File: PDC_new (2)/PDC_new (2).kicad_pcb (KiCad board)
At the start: 2 copper layers, 96 parts, among them J1 Conn_01x02_Pin, J10 Conn_01x02_Pin, J12 Conn_01x02_Pin, J13 XT90PW-F, J14 B2B-XH-A__LF__SN_, J15 Conn_01x02, J2 Conn_01x02_Pin, J3 Conn_01x02_Pin, J4 Conn_01x02_Pin, J5 Conn_01x02_Pin, J6 Conn_01x02_Pin, J7 Conn_01x02_Pin, J8 Conn_01x02_Pin, J9 Conn_01x02_Pin, Q1 BSS123, Q2 IRF540NSTRLPBF, U1 TPSI3050QDWZRQ1, U10 LM393LVDR, U11 IPB017N10N5ATMA1, U12 IPB017N10N5ATMA1, U14 IPB017N10N5ATMA1, U2 TPSI3050QDWZRQ1, U3 TPSI3050QDWZRQ1, U4 74HC74, U5 URB4805LD-60WR3, U6 IPB017N10N5ATMA1, U7 TLC555CDR, U8 SN74HC08D, U9 SN74HC14DR

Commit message: Route PDC_new (2) PCB and swap JST/switch for XT90PW(2+2) connector
Schematic:
- Replace the two JST XH (B2B-XH-A) connectors and the TS-1187A
  tactile switch with a single XT90PW(2+2)-M.G.Y power+signal connector
- Update related passives, power symbols and net labels

PCB:
- Sync footprints with the schematic (drop JST XH and TS-1187A,
  add CONN-TH_XT90PW2X2-MGY)
- Add first routing pass: ~290 track segments and 6 copper zones

Project:
- Adjust design rules: hole clearance 0.25 mm, min via 0.5 mm /
  0.1 mm annular ring, min text 0.8 mm / 0.08 mm thickness
- Clear predefined track width and diff-pair presets

Co-Authored-By: Claude Opus 5.5 <noreply@anthropic.com>
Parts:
- removed C24: 2.2µF, Capacitor_SMD:C_0805_2012Metric
- removed J14: B2B-XH-A__LF__SN_, Connector_JST:JST_XH_B2B-XH-A_1x02_P2.50mm_Vertical
- removed J15: Conn_01x02, Connector_JST:JST_XH_B2B-XH-A_1x02_P2.50mm_Vertical
- removed R28, R29: 10k, Resistor_SMD:R_0805_2012Metric
- removed S1: TS-1187A-B-A-B, TS-1187A-B-A-B:SW_TS-1187A-B-A-B
- added J11: XT90PW(2+2)-M.G.Y, XT90PW(2+2)-M.G.Y:CONN-TH_XT90PW2X2-MGY, F.Cu at (331.0, 272.4)
- moved C2 261.8 mm to (327.0, 187.8)
- moved C1 261.6 mm to (326.9, 167.9)
- moved C3 261.0 mm to (314.5, 227.0), turned to 90 degrees
- moved C4 258.4 mm to (330.5, 212.0), turned to 90 degrees
- moved D3 241.1 mm to (342.3, 223.5), turned to 90 degrees
- moved D1 238.3 mm to (337.8, 223.5), turned to 90 degrees
- moved D7 233.3 mm to (331.5, 256.5)
- moved U5 230.0 mm to (301.0, 249.0), turned to 180 degrees
- moved C6 218.4 mm to (344.3, 240.7), turned to -90 degrees
- moved C5 216.9 mm to (257.7, 268.1), turned to 180 degrees
- moved J12 216.1 mm to (274.5, 267.9), turned to 180 degrees
- moved R2 212.7 mm to (311.1, 208.7), turned to 90 degrees
- moved R31 212.6 mm to (331.5, 261.0), turned to -90 degrees
- moved F2 206.7 mm to (335.2, 231.5), turned to -90 degrees
- moved J6 202.7 mm to (215.2, 251.6), turned to 90 degrees
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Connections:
- F3 pad 1: /BATT+ -> /PRE_FUSE
- F3 pad 2: /PRE_FUSE -> /BATT+
- R25 pad 1: Net-(U10A-OUT1) -> /CMP_FILT
- R25 pad 2: /CMP_FILT -> Net-(U10A-OUT1)
- RV1 pad 2: Net-(U5-0V) -> GND
- RV1 pad 3: Net-(U5-0V) -> GND
- U11 pad 4: /BATT+ -> /BUS+
- U11 pad 7: /BUS+ -> /BATT+
- U12 pad 4: /BATT+ -> /BUS+
- U12 pad 7: /BUS+ -> /BATT+
- U14 pad 4: /BATT+ -> /BUS+
- U14 pad 7: /BUS+ -> /BATT+
- U5 pad 5: Net-(U5-0V) -> GND
- U6 pad 4: /BATT+ -> /BUS+
- U6 pad 7: /BUS+ -> /BATT+
- U9 pad 5: /MSTR_FILT -> GND
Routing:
- net /EN_BLEED: track 0.00 -> 60.9 mm
- net /GATE_MAIN: track 0.00 -> 47.1 mm
- net /RUN_N: track 0.00 -> 44.8 mm
- net /POR_N: track 0.00 -> 41.4 mm
- net /MSTR_ON: track 0.00 -> 38.7 mm
- net /FAULT_N: track 0.00 -> 32.1 mm
- net /PRE_DRAIN: track 0.00 -> 27.2 mm
- net /DONE_N: track 0.00 -> 26.9 mm
- net /BUCK_IN: track 0.00 -> 21.4 mm
- net /EN_MAIN: track 0.00 -> 20.5 mm
- net Net-(D6-K): track 0.00 -> 18.0 mm
- net /RUN_OK: track 0.00 -> 17.7 mm
- net /RUN_CLR_N: track 0.00 -> 15.2 mm
- net /BUCK_OR: track 0.00 -> 15.0 mm
- net /PRE_FUSE: track 0.00 -> 14.1 mm
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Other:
- board outline added: 153 x 129 mm
- copper layers 2 -> 4

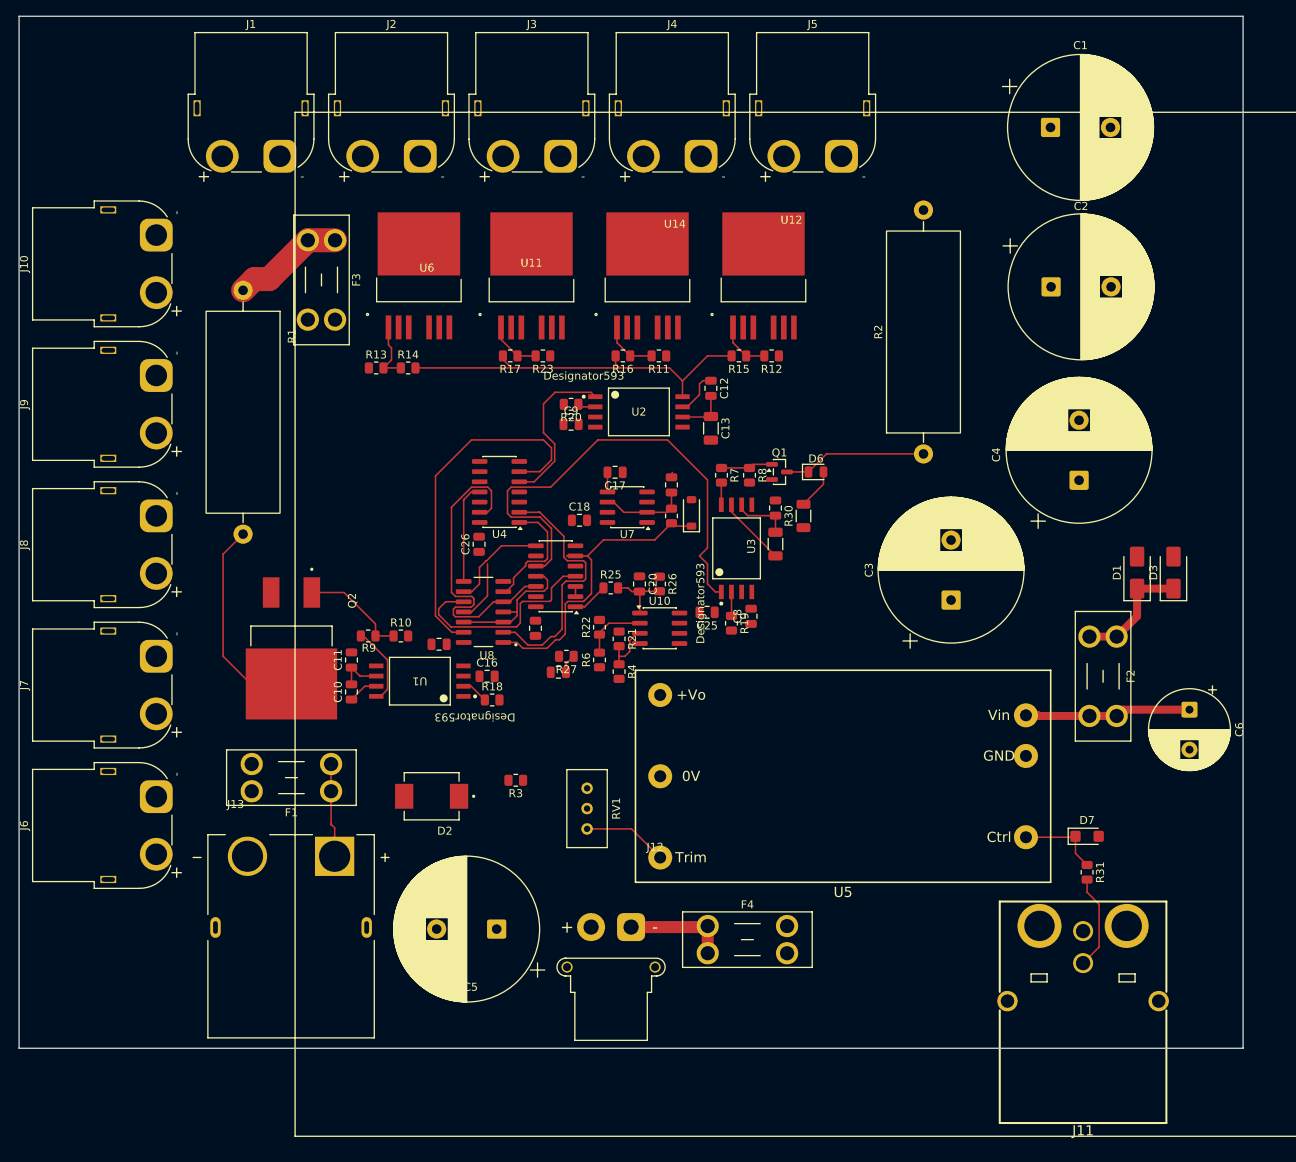
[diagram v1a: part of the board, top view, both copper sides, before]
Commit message: Update PDC_new (2) PCB layout: reposition footprints and reroute tracks
Adjust component placement and silkscreen/graphics, and re-route
affected track segments to match the updated placement.

Co-Authored-By: Claude Opus 5.5 <noreply@anthropic.com>
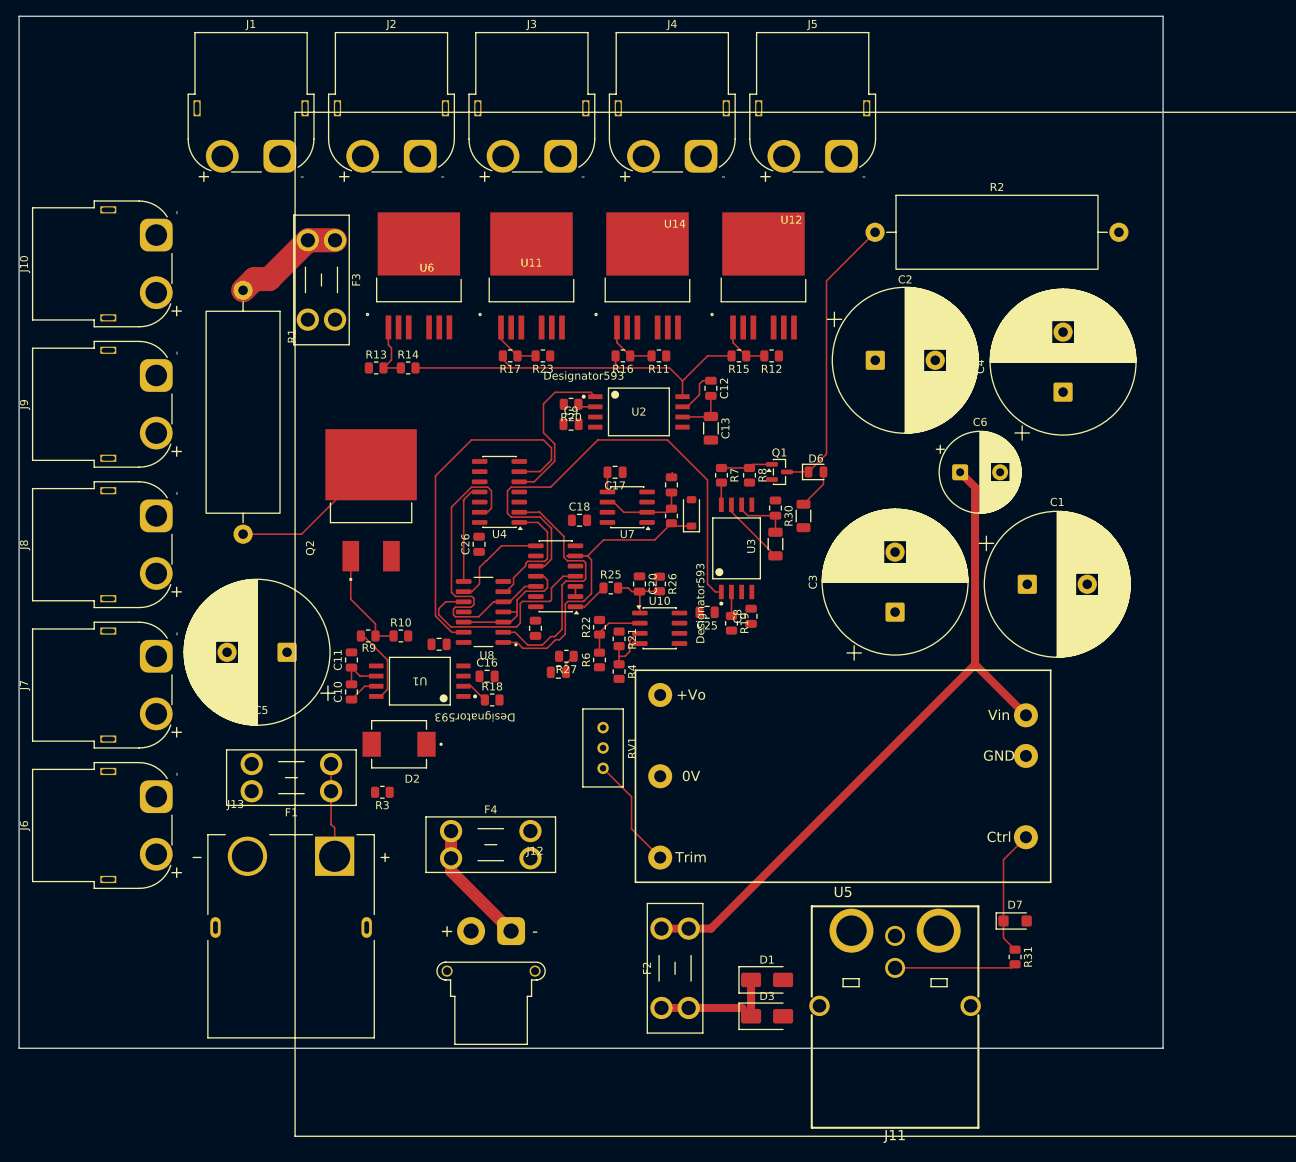
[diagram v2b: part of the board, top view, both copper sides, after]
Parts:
- moved D3 75.2 mm to (291.5, 279.0), turned to 0 degrees
- moved F2 73.4 mm to (278.3, 278.0), turned to 90 degrees
- moved D1 68.8 mm to (291.5, 274.4), turned to 0 degrees
- moved C1 57.2 mm to (324.0, 225.0)
- moved C5 43.4 mm to (231.5, 233.5)
- moved C6 41.3 mm to (315.6, 211.0), turned to 0 degrees
- moved F4 34.2 mm to (252.0, 255.8)
- moved R2 28.4 mm to (305.0, 181.0), turned to 0 degrees
- moved C2 23.8 mm to (305.0, 197.0)
- moved J11 23.5 mm to (307.5, 273.0)
- moved Q2 21.0 mm to (242.0, 214.5), turned to 90 degrees
- moved R3 16.7 mm to (243.4, 251.0)
- moved J12 15.0 mm to (259.5, 268.4)
- moved D7 13.9 mm to (322.5, 267.1)
- moved R31 13.9 mm to (322.5, 271.6)
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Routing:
- net /BUCK_IN: track 21.4 -> 86.9 mm
- net Net-(D6-K): track 18.0 -> 36.1 mm
- net /EN_PRE: track 8.40 -> 0.60 mm
- net /PRE_DRAIN: track 27.2 -> 20.5 mm
- net Net-(J12-Pin_1): track 13.0 -> 19.0 mm
- net /BUCK_CTRL: track 10.4 -> 15.8 mm
- net Net-(U5-Trim): track 10.6 -> 14.1 mm
- net /DET: track 11.9 -> 15.2 mm
- net /BUCK_OR: track 15.0 -> 16.2 mm
- net /EN_BLEED: track 60.9 -> 60.1 mm
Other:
- board size 153 x 129 mm -> 143 x 129 mm

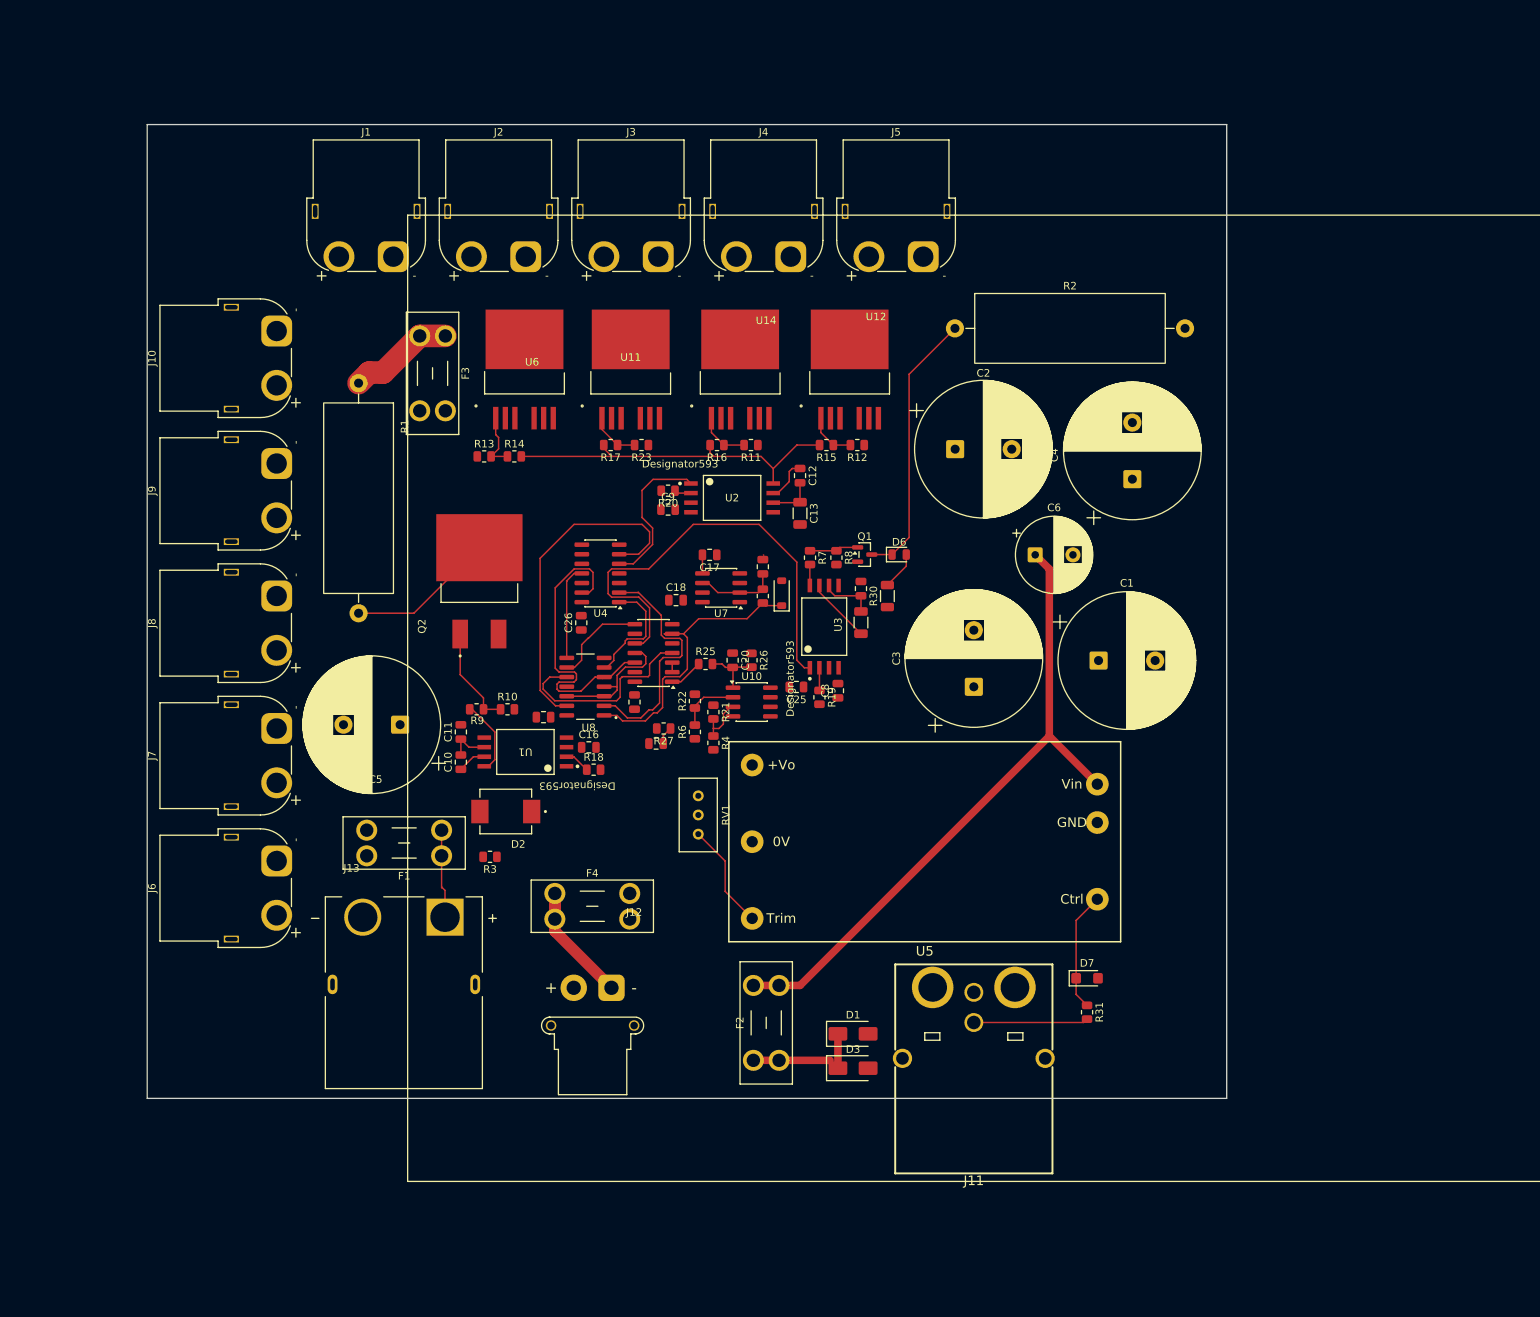
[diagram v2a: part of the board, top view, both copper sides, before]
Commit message: Update PDC_new (2) PCB layout and add XT90PW(2+2) / power part libraries
- Continue routing and layout work on PDC_new (2).kicad_pcb
- Add XT90PW(2+2)-M.G.Y connector symbol/footprint source files
- Add UltraLibrarian import guides for IPB017N10N5ATMA1 and TPSI3050QDWZRQ1
- Ignore 3D model files (*.step, *.stp, *.wrl) so they stay local

Co-Authored-By: Claude Opus 5.5 <noreply@anthropic.com>
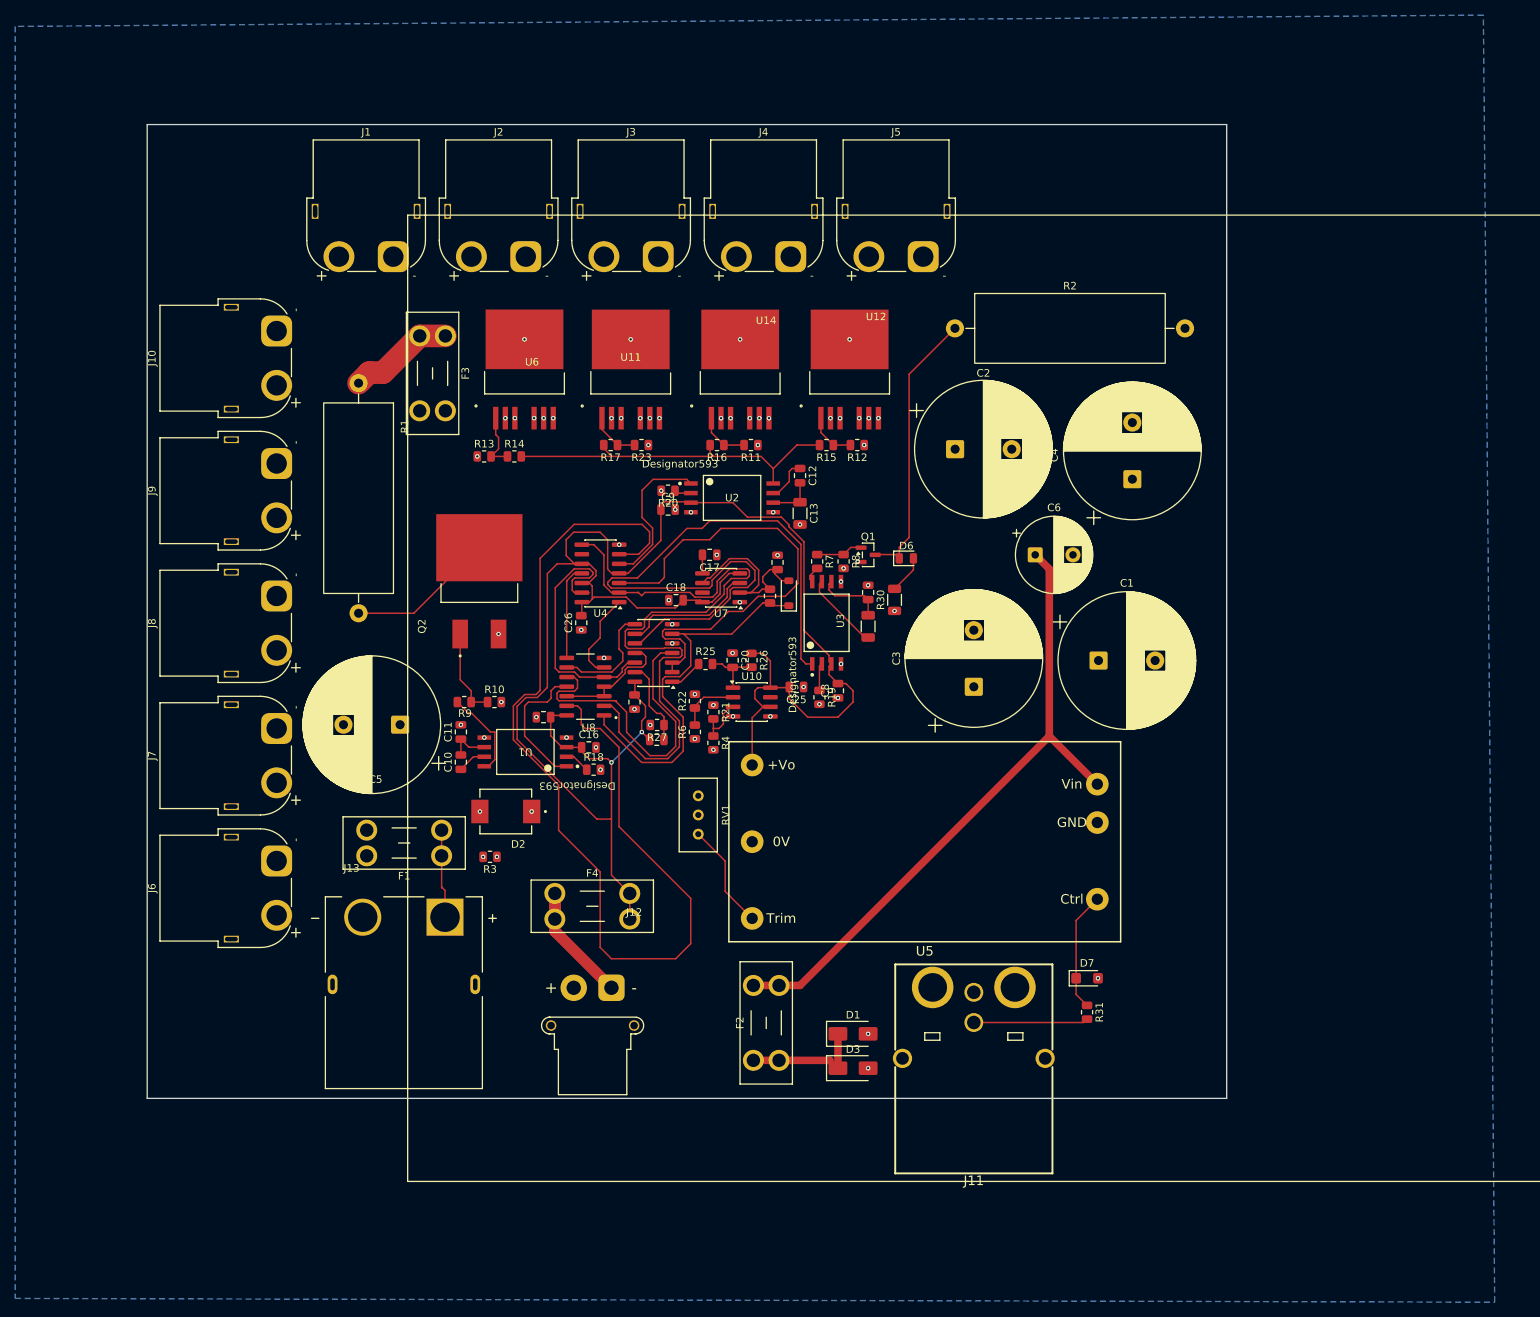
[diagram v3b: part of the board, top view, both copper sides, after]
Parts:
- moved C19 2.03 mm to (281.5, 212.0)
- moved R10 1.97 mm to (244.0, 230.5)
- moved R9 1.90 mm to (240.0, 230.5)
- moved C14 1.07 mm to (293.5, 220.5)
- moved C15 1.07 mm to (293.5, 216.0)
- moved D6 1.07 mm to (298.6, 211.5)
- moved R30 1.07 mm to (297.0, 217.0)
- moved R7 1.07 mm to (286.8, 211.9)
- moved R8 1.07 mm to (290.2, 211.9)
- moved R27 0.98 mm to (265.6, 233.5)
- moved D5 0.95 mm to (283.0, 216.1)
- moved R24 0.95 mm to (280.5, 216.5)
- moved U3 0.60 mm to (288.0, 220.0)
- moved C21 0.51 mm to (265.5, 235.5)
- moved Q1 0.45 mm to (293.5, 211.0)
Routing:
- net /+5V: track 0.00 -> 242.3 mm, vias 0 -> 2
- net /RUN_N: track 44.8 -> 135.3 mm
- net /PC_DONE: track 1.27 -> 63.5 mm
- net /FAULT_N: track 32.1 -> 92.9 mm
- net /EN_BLEED: track 60.1 -> 90.8 mm
- net /EN_PRE: track 0.60 -> 19.0 mm
- net /TMR_OUT: track 0.00 -> 17.9 mm
- net /DONE_N: track 26.9 -> 43.0 mm
- net /TIMER_RC: track 10.7 -> 24.8 mm
- net /MSTR_ON: track 38.7 -> 51.5 mm
- net /POR_RC: track 2.40 -> 11.4 mm
- net /POR_N: track 41.4 -> 37.3 mm
- net /RUN_CLR_N: track 15.2 -> 12.2 mm
- net /TIMEOUT: track 12.6 -> 15.0 mm
- net Net-(U1-VDRV): track 10.2 -> 12.2 mm
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- added copper zone on B.Cu, net /BATT+
- added copper zone on In2.Cu, net /BUS+
- added copper zone on In1.Cu, net GND
